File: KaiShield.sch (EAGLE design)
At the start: 35 parts, among them IC1 MC33269ST-3.3T3, IC2 MCP1700-3302E/TO-ND

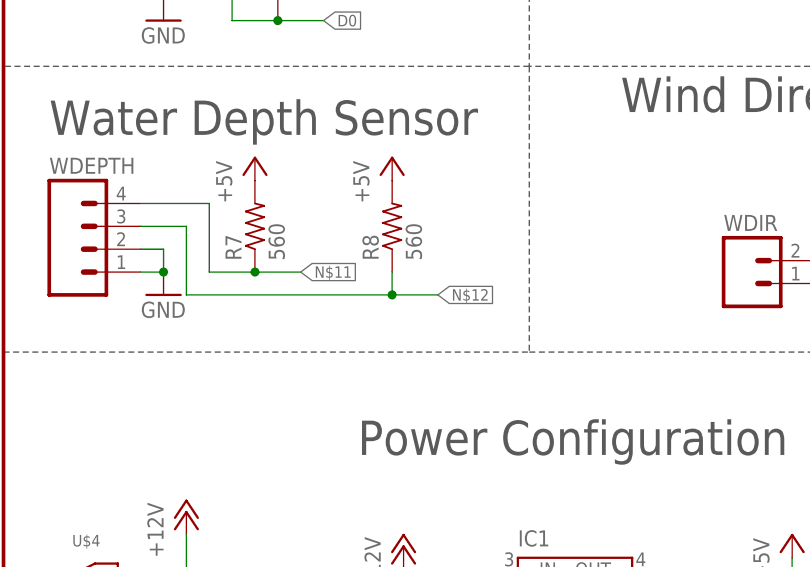
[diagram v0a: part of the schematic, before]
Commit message: Updated KaiShield board and added two more sensors. Now this is the main board instead of just a station board :D.
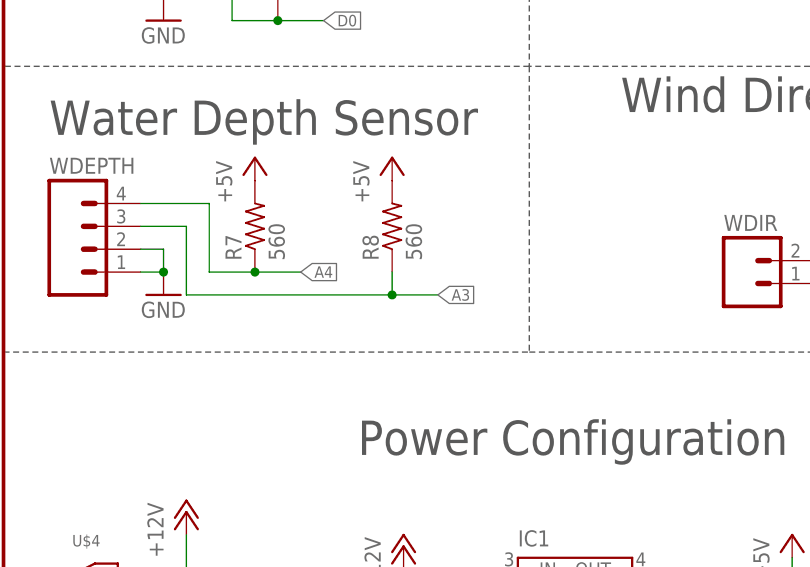
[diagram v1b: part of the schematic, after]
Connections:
- removed net N$11: R7.1, WDEPTH.4
- removed net N$12: R8.1, WDEPTH.3
- net A3: now also R8.1, WDEPTH.3
- net A4: now also R7.1, WDEPTH.4
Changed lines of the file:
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@@
 <pinref part="U$2" gate="G$1" pin="A3"/>
+</segment>
+<segment>
+<pinref part="WDEPTH" gate="G$1" pin="3"/>
+<wire x1="15.24" y1="132.08" x2="20.32" y2="132.08" width="0.1524" layer="91"/>
+<wire x1="20.32" y1="132.08" x2="20.32" y2="124.46" width="0.1524" layer="91"/>
+<wire x1="20.32" y1="124.46" x2="43.18" y2="124.46" width="0.1524" layer="91"/>
+<wire x1="43.18" y1="124.46" x2="43.18" y2="127" width="0.1524" layer="91"/>
+<pinref part="R8" gate="G$1" pin="1"/>
+<wire x1="43.18" y1="124.46" x2="48.26" y2="124.46" width="0.1524" layer="91"/>
+<junction x="43.18" y="124.46"/>
+<label x="48.26" y="124.46" size="1.27" layer="95" xref="yes"/>
 </segment>
 </net>
@@
 <label x="50.8" y="7.62" size="1.27" layer="95" rot="R270" xref="yes"/>
 <pinref part="U$2" gate="G$1" pin="A4"/>
+</segment>
+<segment>
+<pinref part="WDEPTH" gate="G$1" pin="4"/>
+<wire x1="15.24" y1="134.62" x2="22.86" y2="134.62" width="0.1524" layer="91"/>
+<wire x1="22.86" y1="134.62" x2="22.86" y2="127" width="0.1524" layer="91"/>
+<wire x1="22.86" y1="127" x2="27.94" y2="127" width="0.1524" layer="91"/>
+<pinref part="R7" gate="G$1" pin="1"/>
+<wire x1="27.94" y1="127" x2="33.02" y2="127" width="0.1524" layer="91"/>
+<junction x="27.94" y="127"/>
+<label x="33.02" y="127" size="1.27" layer="95" xref="yes"/>
 </segment>
 </net>
@@
 </segment>
 </net>
-<net name="N$11" class="0">
-<segment>
-<pinref part="WDEPTH" gate="G$1" pin="4"/>
-<wire x1="15.24" y1="134.62" x2="22.86" y2="134.62" width="0.1524" layer="91"/>
-<wire x1="22.86" y1="134.62" x2="22.86" y2="127" width="0.1524" layer="91"/>
-<wire x1="22.86" y1="127" x2="27.94" y2="127" width="0.1524" layer="91"/>
-<pinref part="R7" gate="G$1" pin="1"/>
-<wire x1="27.94" y1="127" x2="33.02" y2="127" width="0.1524" layer="91"/>
-<junction x="27.94" y="127"/>
-<label x="33.02" y="127" size="1.27" layer="95" xref="yes"/>
-</segment>
-</net>
-<net name="N$12" class="0">
-<segment>
-<pinref part="WDEPTH" gate="G$1" pin="3"/>
-<wire x1="15.24" y1="132.08" x2="20.32" y2="132.08" width="0.1524" layer="91"/>
-<wire x1="20.32" y1="132.08" x2="20.32" y2="124.46" width="0.1524" layer="91"/>
-<wire x1="20.32" y1="124.46" x2="43.18" y2="124.46" width="0.1524" layer="91"/>
-<wire x1="43.18" y1="124.46" x2="43.18" y2="127" width="0.1524" layer="91"/>
-<pinref part="R8" gate="G$1" pin="1"/>
-<wire x1="43.18" y1="124.46" x2="48.26" y2="124.46" width="0.1524" layer="91"/>
-<junction x="43.18" y="124.46"/>
-<label x="48.26" y="124.46" size="1.27" layer="95" xref="yes"/>
-</segment>
-</net>

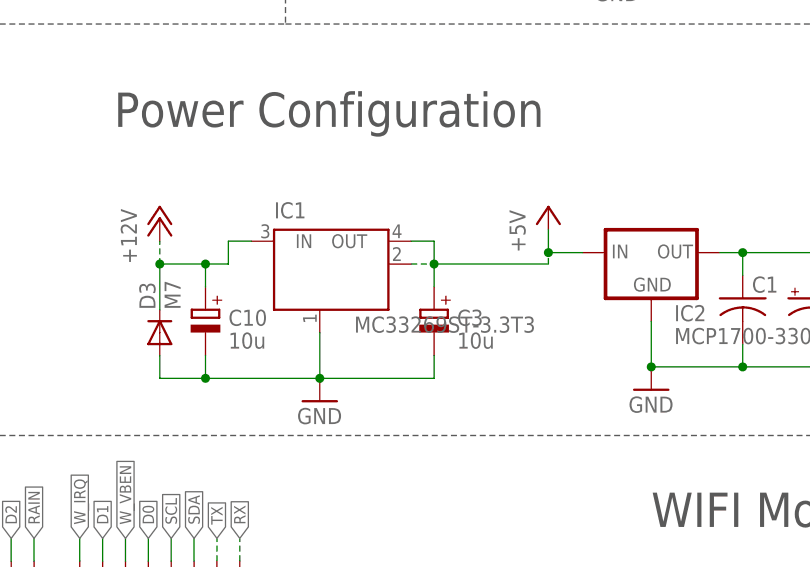
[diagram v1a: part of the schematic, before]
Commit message: updated KaiShield with the new power ic foot print DPAK
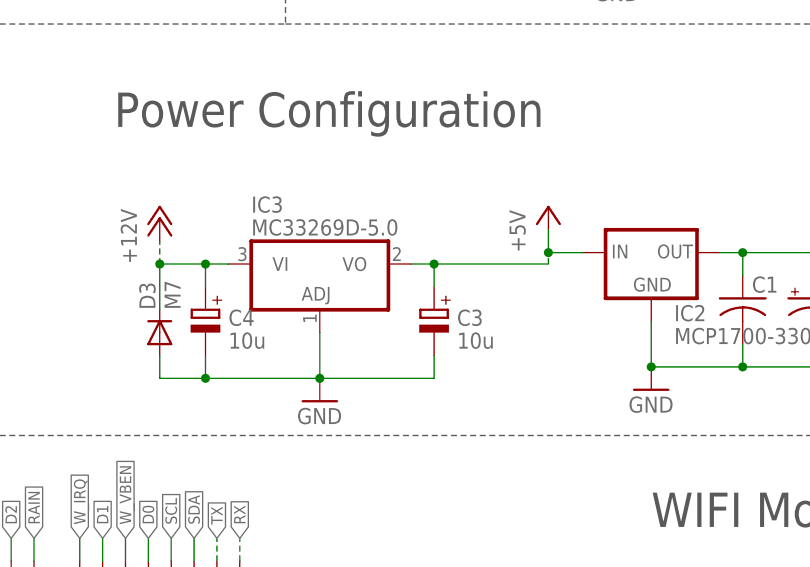
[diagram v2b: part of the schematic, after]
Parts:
- removed IC1: MC33269ST-3.3T3, linear:MC33269ST-3.3T3
- added IC3: MC33269D-5.0, linear:MC33269D-5.0
- renumbered C10 to C4
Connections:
- net +12V: now also IC3.VI; no longer IC1.IN
- net +5V: now also IC3.VO; no longer IC1.OUT, IC1.OUT@1
- net GND: now also IC3.ADJ; no longer IC1.GND/ADJ
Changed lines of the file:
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@@
 <setting verticaltext="up"/>
 </settings>
-<grid distance="0.1" unitdist="inch" unit="inch" style="lines" multiple="1" display="no" altdistance="0.01" altunitdist="inch" altunit="inch"/>
+<grid distance="0.05" unitdist="inch" unit="inch" style="lines" multiple="1" display="no" altdistance="0.01" altunitdist="inch" altunit="inch"/>
 <layers>
 <layer number="1" name="Top" color="4" fill="1" visible="no" active="no"/>
@@
 <part name="GND7" library="supply1" deviceset="GND" device=""/>
 <part name="D3" library="diode" deviceset="DIODE-" device="SMB" value="M7"/>
-<part name="C10" library="rcl" deviceset="CPOL-EU" device="SMCB" value="10u"/>
+<part name="C4" library="rcl" deviceset="CPOL-EU" device="SMCB" value="10u"/>
 <part name="C3" library="rcl" deviceset="CPOL-EU" device="SMCB" value="10u"/>
-<part name="IC1" library="linear" deviceset="MC33269ST*" device="" technology="-3.3T3"/>
 <part name="U$4" library="adafruit" deviceset="2.1MMJACK" device="THM"/>
 <part name="WDEPTH" library="SparkFun-Connectors" deviceset="M04" device="PTH"/>
@@
 <part name="P+7" library="supply1" deviceset="+5V" device=""/>
 <part name="P+8" library="supply1" deviceset="+5V" device=""/>
+<part name="IC3" library="linear" deviceset="MC33269?*" device="D" technology="-5.0"/>
 </parts>
 <sheets>
@@
 <instance part="GND7" gate="1" x="62.23" y="76.2"/>
 <instance part="D3" gate="G$1" x="44.45" y="83.82" rot="R90"/>
-<instance part="C10" gate="G$1" x="49.53" y="86.36" smashed="yes" rot="MR0">
+<instance part="C4" gate="G$1" x="49.53" y="86.36" smashed="yes" rot="MR0">
 <attribute name="NAME" x="52.07" y="86.36" size="1.778" layer="95" rot="MR180"/>
 <attribute name="VALUE" x="52.07" y="83.82" size="1.778" layer="96" rot="MR180"/>
@@
 <attribute name="VALUE" x="77.47" y="83.82" size="1.778" layer="96" rot="MR180"/>
 </instance>
-<instance part="IC1" gate="G$1" x="62.23" y="88.9"/>
 <instance part="U$4" gate="G$1" x="10.16" y="91.44"/>
 <instance part="WDEPTH" gate="G$1" x="10.16" y="129.54"/>
@@
 <instance part="P+7" gate="1" x="27.94" y="139.7"/>
 <instance part="P+8" gate="1" x="43.18" y="139.7"/>
+<instance part="IC3" gate="G$1" x="62.23" y="88.9"/>
 </instances>
 <busses>
@@
 <segment>
 <pinref part="GND7" gate="1" pin="GND"/>
-<wire x1="62.23" y1="78.74" x2="62.23" y2="83.82" width="0.1524" layer="91"/>
-<pinref part="C10" gate="G$1" pin="-"/>
+<pinref part="C4" gate="G$1" pin="-"/>
 <wire x1="49.53" y1="78.74" x2="49.53" y2="81.28" width="0.1524" layer="91"/>
 <pinref part="D3" gate="G$1" pin="A"/>
@@
 <pinref part="C3" gate="G$1" pin="-"/>
 <wire x1="74.93" y1="78.74" x2="74.93" y2="81.28" width="0.1524" layer="91"/>
-<pinref part="IC1" gate="G$1" pin="GND/ADJ"/>
+<pinref part="IC3" gate="G$1" pin="ADJ"/>
+<wire x1="62.23" y1="83.82" x2="62.23" y2="78.74" width="0.1524" layer="91"/>
 </segment>
 <segment>
@@
 <wire x1="87.63" y1="91.44" x2="87.63" y2="92.71" width="0.1524" layer="91" style="longdash"/>
 <junction x="87.63" y="92.71"/>
-<wire x1="72.39" y1="91.44" x2="74.93" y2="91.44" width="0.1524" layer="91" style="longdash"/>
 <wire x1="74.93" y1="88.9" x2="74.93" y2="91.44" width="0.1524" layer="91"/>
 <pinref part="C3" gate="G$1" pin="+"/>
 <wire x1="87.63" y1="91.44" x2="74.93" y2="91.44" width="0.1524" layer="91"/>
 <junction x="74.93" y="91.44"/>
-<pinref part="IC1" gate="G$1" pin="OUT@1"/>
-<pinref part="IC1" gate="G$1" pin="OUT"/>
-<wire x1="72.39" y1="93.98" x2="74.93" y2="93.98" width="0.1524" layer="91"/>
-<wire x1="74.93" y1="93.98" x2="74.93" y2="91.44" width="0.1524" layer="91"/>
+<pinref part="IC3" gate="G$1" pin="VO"/>
+<wire x1="72.39" y1="91.44" x2="74.93" y2="91.44" width="0.1524" layer="91"/>
 </segment>
 <segment>
@@
 <pinref part="D3" gate="G$1" pin="C"/>
 <wire x1="44.45" y1="86.36" x2="44.45" y2="91.44" width="0.1524" layer="91"/>
+<junction x="44.45" y="91.44"/>
+<pinref part="C4" gate="G$1" pin="+"/>
 <wire x1="52.07" y1="91.44" x2="49.53" y2="91.44" width="0.1524" layer="91"/>
-<junction x="44.45" y="91.44"/>
-<pinref part="C10" gate="G$1" pin="+"/>
 <wire x1="49.53" y1="91.44" x2="44.45" y2="91.44" width="0.1524" layer="91"/>
 <wire x1="49.53" y1="88.9" x2="49.53" y2="91.44" width="0.1524" layer="91"/>
 <junction x="49.53" y="91.44"/>
-<pinref part="IC1" gate="G$1" pin="IN"/>
-<wire x1="54.61" y1="93.98" x2="52.07" y2="93.98" width="0.1524" layer="91"/>
-<wire x1="52.07" y1="93.98" x2="52.07" y2="91.44" width="0.1524" layer="91"/>
-</segment>
-<segment>
+<pinref part="IC3" gate="G$1" pin="VI"/>
+</segment>
+<segment>
